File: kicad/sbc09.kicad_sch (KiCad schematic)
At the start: 77 parts, among them J1 Conn_01x03_Male, J2 Conn_01x06_Male, J3 Conn_01x06_Male, J4 Conn_01x06_Male, J5 Conn_02x05_Odd_Even, J6 Conn_02x25_Odd_Even, Q1 2N7000, SW1 SW_Push, U1 74LS245, U10 74LS670, U11 74LS670, U12 AS6C4008-55PCN, U13 SST39SF040-DIP, U14 SST39SF040-DIP, U15 XR68C681CJ, U16 MAX232, U2 74LS245, U3 74LS245, U4 MC6809E, U5 74HCT125, U6 ATF22V10C, U7 ATF22V10C, U8 74LS670, U9 74LS670, X1 8MHz, X2 3.6864MHz

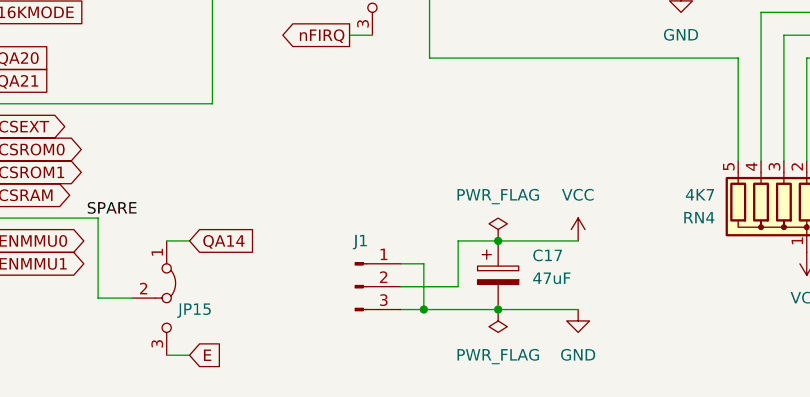
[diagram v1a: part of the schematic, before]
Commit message: Replace J1 (ext power) with Molex KK
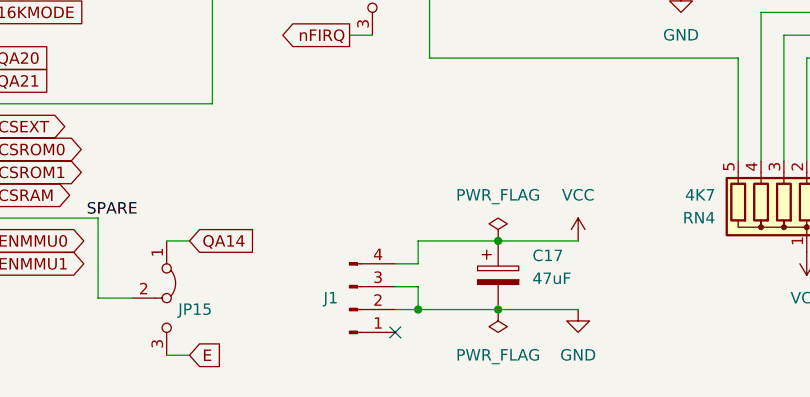
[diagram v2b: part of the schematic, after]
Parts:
- removed J1: Conn_01x03_Male, Connector_PinHeader_2.54mm:PinHeader_1x03_P2.54mm_Vertical, symbol Connector:Conn_01x03_Male
- added J1: (no value), symbol Connector:Conn_01x04_Male
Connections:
- net GND: now also J1.2 (Pin_2), J1.3 (Pin_3)
- net VCC: now also J1.4 (Pin_4)
- no-connect marks 15 -> 16
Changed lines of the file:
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@@
   (junction (at 35.56 34.29) (diameter 0) (color 0 0 0 0)
   )
+  (junction (at 125.73 276.86) (diameter 0) (color 0 0 0 0)
+  )
   (junction (at 156.21 19.05) (diameter 0) (color 0 0 0 0)
   )
@@
   (junction (at 26.67 40.64) (diameter 0) (color 0 0 0 0)
   )
-  (junction (at 126.365 276.86) (diameter 0) (color 0 0 0 0)
-  )
   (junction (at 33.02 166.37) (diameter 0) (color 0 0 0 0)
   )
@@
   (junction (at 246.38 248.92) (diameter 0) (color 0 0 0 0)
   )
+  (no_connect (at 123.19 279.4))
   (no_connect (at 377.19 219.71))
   (no_connect (at 129.54 231.14))
@@
     (stroke (width 0) (type default) (color 0 0 0 0))
   )
-  (wire (pts (xy 227.33 256.54) (xy 240.03 256.54))
+  (wire (pts (xy 125.73 269.24) (xy 134.62 269.24))
     (stroke (width 0) (type default) (color 0 0 0 0))
   )
-  (wire (pts (xy 130.175 269.24) (xy 134.62 269.24))
+  (wire (pts (xy 227.33 256.54) (xy 240.03 256.54))
     (stroke (width 0) (type default) (color 0 0 0 0))
   )
@@
     (stroke (width 0) (type default) (color 0 0 0 0))
   )
+  (wire (pts (xy 125.73 271.78) (xy 125.73 269.24))
+    (stroke (width 0) (type default) (color 0 0 0 0))
+  )
   (wire (pts (xy 195.58 218.44) (xy 217.17 218.44))
     (stroke (width 0) (type default) (color 0 0 0 0))
@@
     (stroke (width 0) (type default) (color 0 0 0 0))
   )
-  (wire (pts (xy 123.825 276.86) (xy 126.365 276.86))
-    (stroke (width 0) (type default) (color 0 0 0 0))
-  )
   (wire (pts (xy 389.89 219.71) (xy 400.05 219.71))
     (stroke (width 0) (type default) (color 0 0 0 0))
@@
     (stroke (width 0) (type default) (color 0 0 0 0))
   )
-  (wire (pts (xy 130.175 274.32) (xy 123.825 274.32))
-    (stroke (width 0) (type default) (color 0 0 0 0))
-  )
   (wire (pts (xy 302.26 180.34) (xy 302.26 181.61))
     (stroke (width 0) (type default) (color 0 0 0 0))
@@
     (stroke (width 0) (type default) (color 0 0 0 0))
   )
-  (wire (pts (xy 126.365 276.86) (xy 134.62 276.86))
-    (stroke (width 0) (type default) (color 0 0 0 0))
-  )
   (wire (pts (xy 295.91 73.66) (xy 312.42 73.66))
     (stroke (width 0) (type default) (color 0 0 0 0))
@@
     (stroke (width 0) (type default) (color 0 0 0 0))
   )
+  (wire (pts (xy 123.19 274.32) (xy 125.73 274.32))
+    (stroke (width 0) (type default) (color 0 0 0 0))
+  )
   (wire (pts (xy 52.07 78.74) (xy 48.26 78.74))
     (stroke (width 0) (type default) (color 0 0 0 0))
@@
     (stroke (width 0) (type default) (color 0 0 0 0))
   )
+  (wire (pts (xy 123.19 271.78) (xy 125.73 271.78))
+    (stroke (width 0) (type default) (color 0 0 0 0))
+  )
   (wire (pts (xy 337.82 53.34) (xy 342.9 53.34))
     (stroke (width 0) (type default) (color 0 0 0 0))
@@
     (stroke (width 0) (type default) (color 0 0 0 0))
   )
+  (wire (pts (xy 125.73 276.86) (xy 134.62 276.86))
+    (stroke (width 0) (type default) (color 0 0 0 0))
+  )
   (wire (pts (xy 100.33 269.24) (xy 97.79 269.24))
     (stroke (width 0) (type default) (color 0 0 0 0))
@@
     (stroke (width 0) (type default) (color 0 0 0 0))
   )
+  (wire (pts (xy 125.73 274.32) (xy 125.73 276.86))
+    (stroke (width 0) (type default) (color 0 0 0 0))
+  )
   (wire (pts (xy 340.36 71.12) (xy 337.82 71.12))
     (stroke (width 0) (type default) (color 0 0 0 0))
@@
     (stroke (width 0) (type default) (color 0 0 0 0))
   )
-  (wire (pts (xy 123.825 271.78) (xy 126.365 271.78))
-    (stroke (width 0) (type default) (color 0 0 0 0))
-  )
   (wire (pts (xy 26.67 40.64) (xy 17.78 40.64))
     (stroke (width 0) (type default) (color 0 0 0 0))
@@
     (stroke (width 0) (type default) (color 0 0 0 0))
   )
+  (wire (pts (xy 123.19 276.86) (xy 125.73 276.86))
+    (stroke (width 0) (type default) (color 0 0 0 0))
+  )
   (bus (pts (xy 369.57 176.53) (xy 369.57 179.07))
     (stroke (width 0) (type default) (color 0 0 0 0))
@@
     (stroke (width 0) (type default) (color 0 0 0 0))
   )
-  (wire (pts (xy 126.365 271.78) (xy 126.365 276.86))
-    (stroke (width 0) (type default) (color 0 0 0 0))
-  )
   (wire (pts (xy 396.24 50.8) (xy 401.32 50.8))
     (stroke (width 0) (type default) (color 0 0 0 0))
@@
     (stroke (width 0) (type default) (color 0 0 0 0))
   )
-  (wire (pts (xy 130.175 274.32) (xy 130.175 269.24))
-    (stroke (width 0) (type default) (color 0 0 0 0))
-  )
   (bus (pts (xy 208.28 38.1) (xy 208.28 40.64))
     (stroke (width 0) (type default) (color 0 0 0 0))
@@
     (pin "1")
   )
-  (symbol (lib_id "Connector:Conn_01x03_Male") (at 118.745 274.32 0) (unit 1)
-    (in_bom yes) (on_board yes) (fields_autoplaced)
-    (property "Reference" "J1" (id 0) (at 119.38 269.24 0))
-    (property "Value" "Conn_01x03_Male" (id 1) (at 119.38 269.24 0)
-      (effects (font (size 1.27 1.27)) hide)
-    )
-    (property "Footprint" "Connector_PinHeader_2.54mm:PinHeader_1x03_P2.54mm_Vertical" (id 2) (at 118.745 274.32 0)
-      (effects (font (size 1.27 1.27)) hide)
-    )
-    (property "Datasheet" "~" (id 3) (at 118.745 274.32 0)
-      (effects (font (size 1.27 1.27)) hide)
-    )
-    (pin "1")
-    (pin "2")
-    (pin "3")
-  )
   (symbol (lib_id "power:GND") (at 185.42 269.24 0) (unit 1)
     (in_bom yes) (on_board yes) (fields_autoplaced)
@@
     (pin "3")
   )
+  (symbol (lib_id "Connector:Conn_01x04_Male") (at 118.11 276.86 0) (mirror x) (unit 1)
+    (in_bom yes) (on_board yes) (fields_autoplaced)
+    (property "Reference" "J1" (id 0) (at 116.84 275.5899 0)
+      (effects (font (size 1.27 1.27)) (justify right))
+    )
+    (property "Value" "" (id 1) (at 118.745 281.94 0)
+      (effects (font (size 1.27 1.27)) hide)
+    )
+    (property "Footprint" "" (id 2) (at 118.11 276.86 0)
+      (effects (font (size 1.27 1.27)) hide)
+    )
+    (property "Datasheet" "~" (id 3) (at 118.11 276.86 0)
+      (effects (font (size 1.27 1.27)) hide)
+    )
+    (pin "1")
+    (pin "2")
+    (pin "3")
+    (pin "4")
+  )
   (symbol (lib_id "Device:R_Network08") (at 25.4 105.41 90) (mirror x) (unit 1)
     (in_bom yes) (on_board yes)
@@
       (reference "H4") (unit 1) (value "2.7mm") (footprint "MountingHole:MountingHole_2.7mm")
     )
-    (path "/2d3bef94-9857-4263-bb09-146a0d34f7ef"
-      (reference "J1") (unit 1) (value "Conn_01x03_Male") (footprint "Connector_PinHeader_2.54mm:PinHeader_1x03_P2.54mm_Vertical")
+    (path "/d7ab0ff9-7261-48ad-92eb-b63b9921aed9"
+      (reference "J1") (unit 1) (value "Conn_01x04_Male") (footprint "Connector_Molex:Molex_KK-254_AE-6410-04A_1x04_P2.54mm_Vertical")
     )
     (path "/c8679364-5ecf-4ff5-92b0-70a3c93f3773"

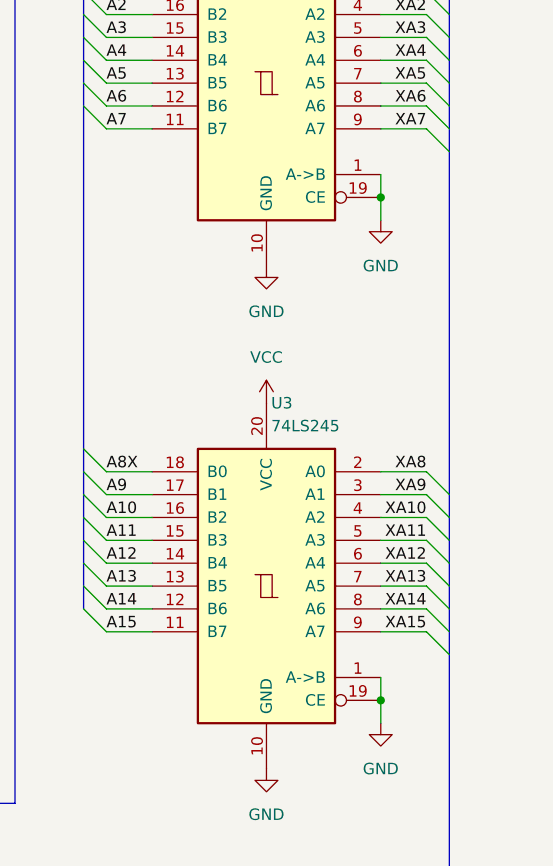
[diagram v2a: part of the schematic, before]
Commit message: Control direction of Addr buffers from BA
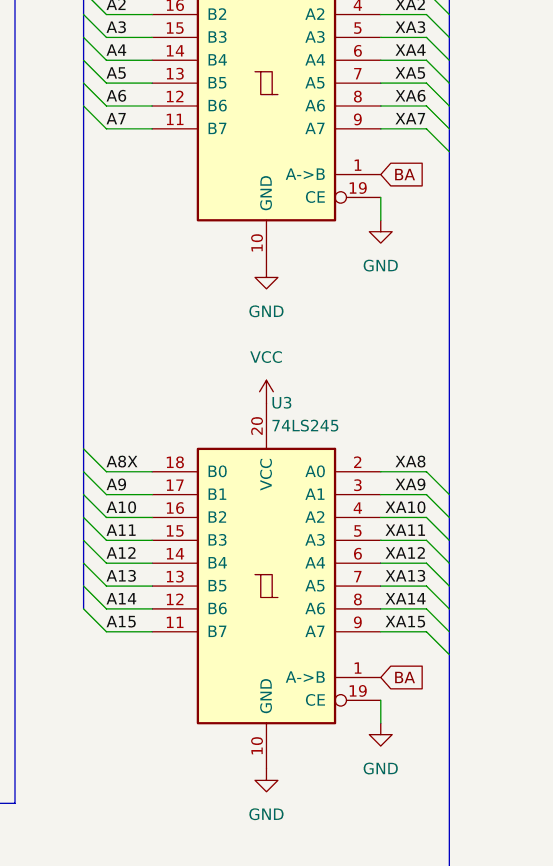
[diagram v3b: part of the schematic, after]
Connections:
- net BA: now also U2.1 (A->B), U3.1 (A->B)
- net GND: no longer U2.1 (A->B), U3.1 (A->B)
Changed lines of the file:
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@@
   (junction (at 246.38 256.54) (diameter 0) (color 0 0 0 0)
   )
-  (junction (at 396.24 60.96) (diameter 0) (color 0 0 0 0)
-  )
   (junction (at 264.16 154.305) (diameter 0) (color 0 0 0 0)
   )
@@
   (junction (at 74.93 153.67) (diameter 0) (color 0 0 0 0)
   )
-  (junction (at 396.24 116.84) (diameter 0) (color 0 0 0 0)
-  )
   (junction (at 240.03 270.51) (diameter 0) (color 0 0 0 0)
   )
@@
     (stroke (width 0) (type default) (color 0 0 0 0))
   )
-  (wire (pts (xy 396.24 114.3) (xy 396.24 116.84))
-    (stroke (width 0) (type default) (color 0 0 0 0))
-  )
   (bus (pts (xy 256.54 40.64) (xy 256.54 43.18))
     (stroke (width 0) (type default) (color 0 0 0 0))
@@
     (stroke (width 0) (type default) (color 0 0 0 0))
   )
-  (wire (pts (xy 396.24 58.42) (xy 396.24 60.96))
-    (stroke (width 0) (type default) (color 0 0 0 0))
-  )
   (wire (pts (xy 49.53 96.52) (xy 52.07 96.52))
     (stroke (width 0) (type default) (color 0 0 0 0))
@@
     )
   )
+  (global_label "BA" (shape input) (at 396.24 58.42 0) (fields_autoplaced)
+    (effects (font (size 1.27 1.27)) (justify left))
+    (property "Intersheet References" "${INTERSHEET_REFS}" (id 0) (at 401.0117 58.3406 0)
+      (effects (font (size 1.27 1.27)) (justify left) hide)
+    )
+  )
   (global_label "Q" (shape input) (at 49.53 99.06 180) (fields_autoplaced)
     (effects (font (size 1.27 1.27)) (justify right))
@@
       (effects (font (size 1.27 1.27)) (justify left) hide)
     )
+  )
+  (global_label "BA" (shape input) (at 396.24 114.3 0) (fields_autoplaced)
+    (effects (font (size 1.27 1.27)) (justify left))
+    (property "Intersheet References" "${INTERSHEET_REFS}" (id 0) (at 401.0117 114.2206 0)
+      (effects (font (size 1.27 1.27)) (justify left) hide)
+    )

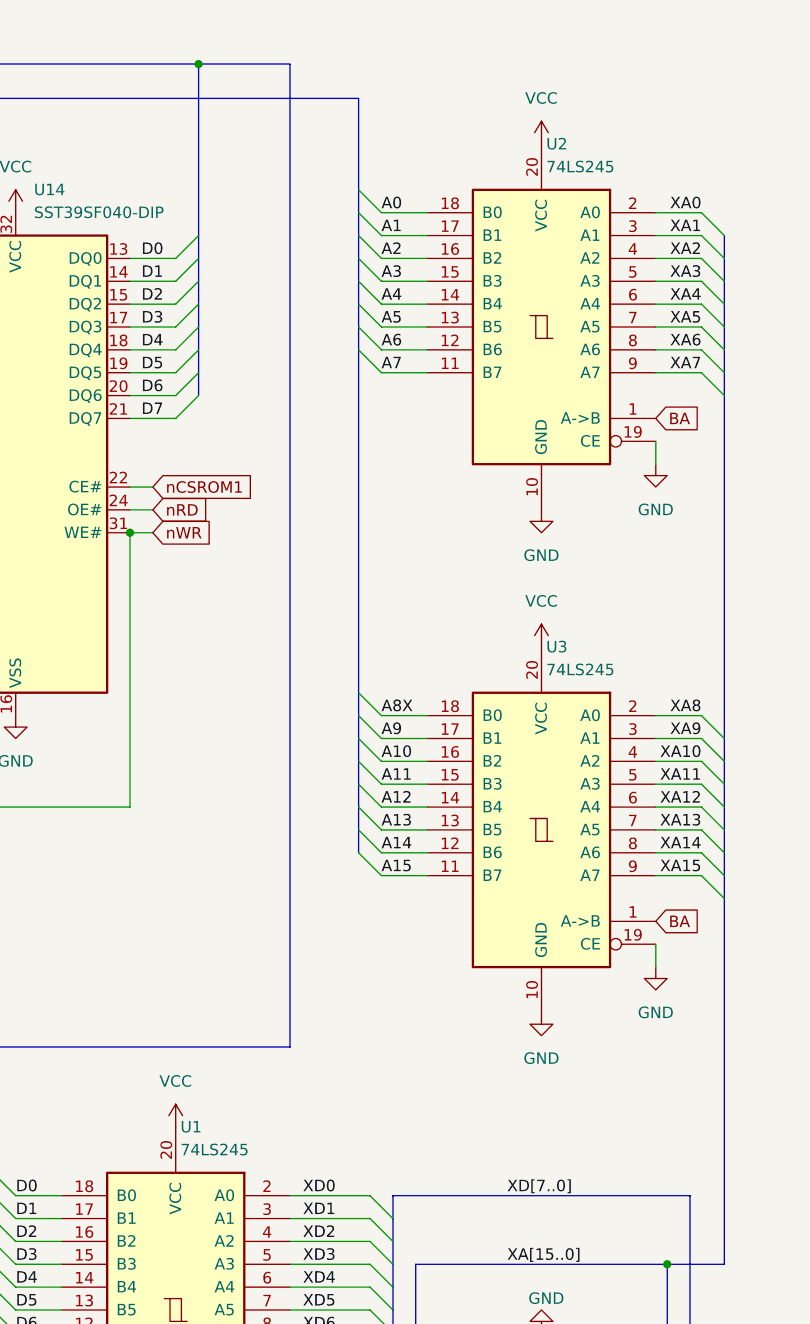
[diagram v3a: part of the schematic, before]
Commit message: Change value of U1/2/3 to 74HCT245
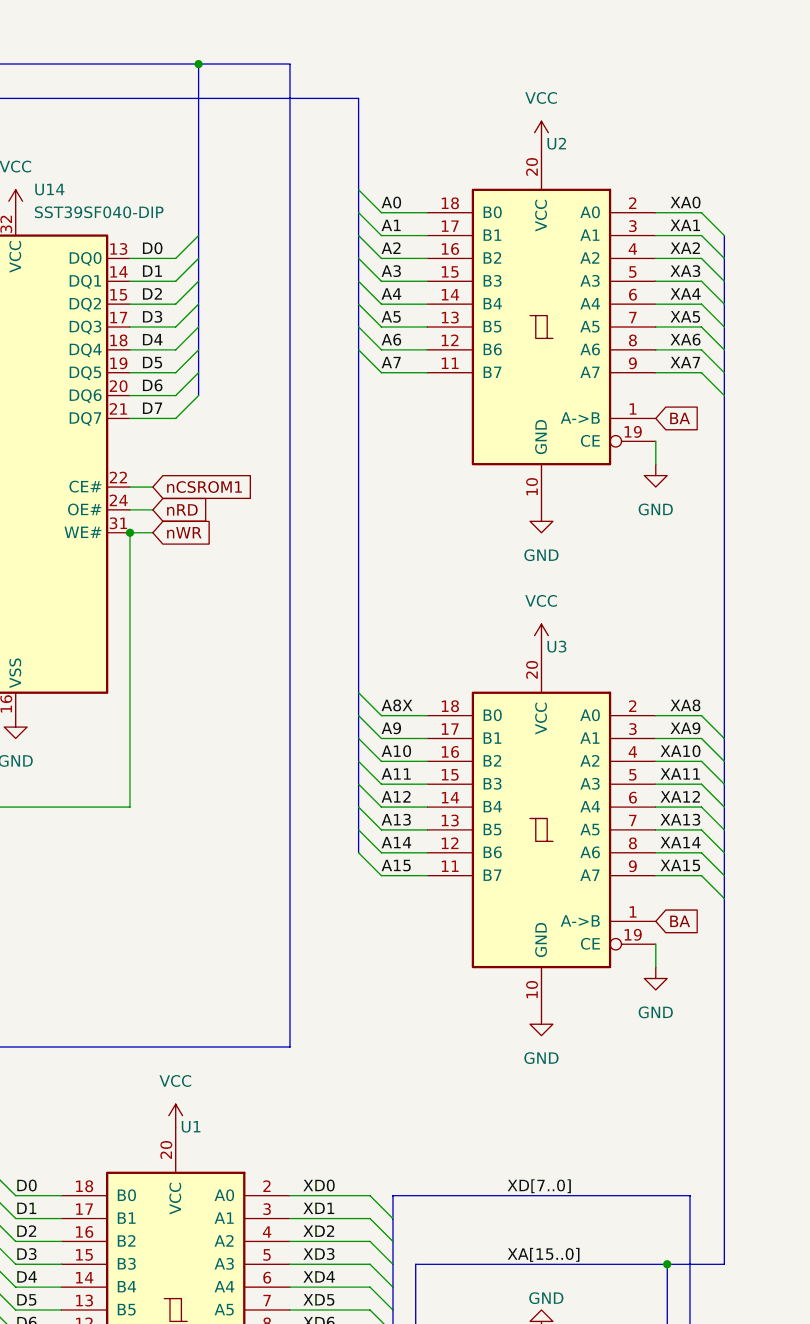
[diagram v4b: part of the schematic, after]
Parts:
- U1, U2, U3: value 74LS245 -> (none)
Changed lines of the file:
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@@
       (effects (font (size 1.27 1.27)) (justify right))
     )
-    (property "Value" "74LS245" (id 1) (at 384.0606 86.36 0)
+    (property "Value" "" (id 1) (at 384.0606 86.36 0)
       (effects (font (size 1.27 1.27)) (justify right))
     )
@@
       (effects (font (size 1.27 1.27)) (justify right))
     )
-    (property "Value" "74LS245" (id 1) (at 384.0606 30.48 0)
+    (property "Value" "" (id 1) (at 384.0606 30.48 0)
       (effects (font (size 1.27 1.27)) (justify right))
     )
@@
       (effects (font (size 1.27 1.27)) (justify right))
     )
-    (property "Value" "74LS245" (id 1) (at 343.4206 139.7 0)
+    (property "Value" "" (id 1) (at 343.4206 139.7 0)
       (effects (font (size 1.27 1.27)) (justify right))
     )
@@
     )
     (path "/b94ab99f-52e3-4ccf-b6fb-e7021a9f054f"
-      (reference "U1") (unit 1) (value "74LS245") (footprint "Package_DIP:DIP-20_W7.62mm_Socket")
+      (reference "U1") (unit 1) (value "74HCT245") (footprint "Package_DIP:DIP-20_W7.62mm_Socket")
     )
     (path "/ac5972a1-fe98-469b-83c0-ddd983b35429"
-      (reference "U2") (unit 1) (value "74LS245") (footprint "Package_DIP:DIP-20_W7.62mm_Socket")
+      (reference "U2") (unit 1) (value "74HCT245") (footprint "Package_DIP:DIP-20_W7.62mm_Socket")
     )
     (path "/8faef091-bd23-44f5-86d7-3dbb33eb4c2b"
-      (reference "U3") (unit 1) (value "74LS245") (footprint "Package_DIP:DIP-20_W7.62mm_Socket")
+      (reference "U3") (unit 1) (value "74HCT245") (footprint "Package_DIP:DIP-20_W7.62mm_Socket")
     )
     (path "/625a12c3-d955-4962-8e19-1bdba92d86fb"

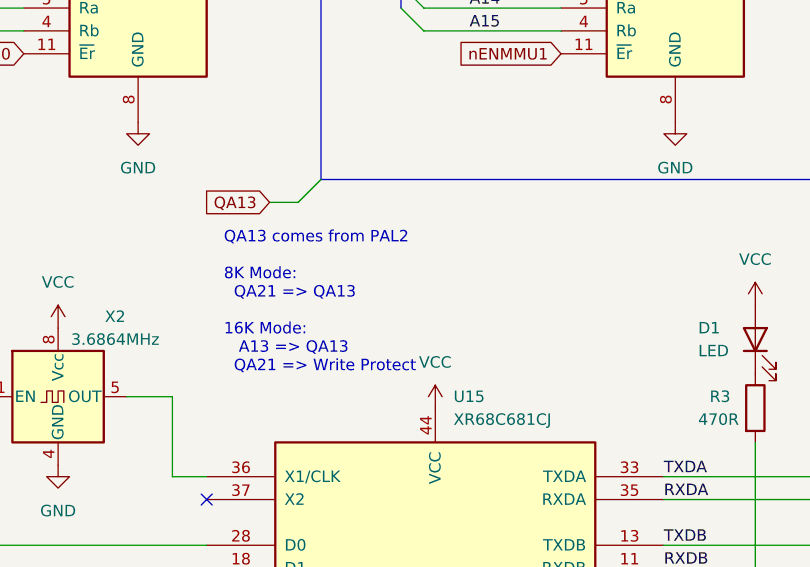
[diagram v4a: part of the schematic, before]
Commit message: Correct comment on schematic
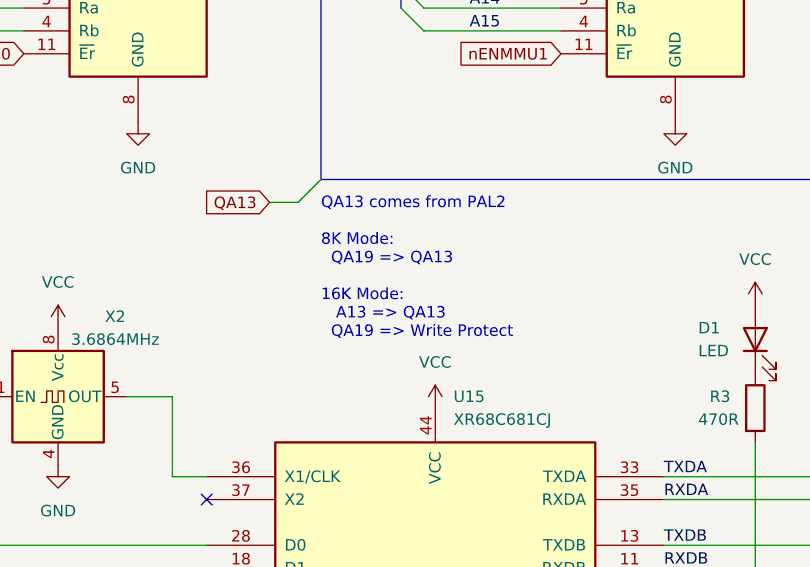
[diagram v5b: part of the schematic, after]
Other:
- note added: "QA13 comes from PAL2 8K Mode: QA19 => QA13 16K Mode: A13 => QA13 QA19 => Write Protect"
- note removed: "QA13 comes from PAL2 8K Mode: QA21 => QA13 16K Mode: A13 => QA13 QA21 => Write Protect"
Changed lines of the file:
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@@
     (effects (font (size 1.27 1.27)) (justify left bottom))
   )
-  (text "QA13 comes from PAL2\n\n8K Mode:\n  QA21 => QA13\n\n16K Mode:\n   A13 => QA13\n  QA21 => Write Protect\n"
-    (at 131.445 163.83 0)
+  (text "QA13 comes from PAL2\n\n8K Mode:\n  QA19 => QA13\n\n16K Mode:\n   A13 => QA13\n  QA19 => Write Protect\n"
+    (at 142.24 160.02 0)
     (effects (font (size 1.27 1.27)) (justify left bottom))
   )

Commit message: KiCAD: Added PAL3 and updated layout
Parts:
- added U17: GAL16V8, Package_DIP:DIP-20_W7.62mm_Socket, symbol Logic_Programmable:GAL16V8
- J1: value (none) -> Conn_01x04_Male; footprint (none) -> Connector_Molex:Molex_KK-254_AE-6410-04A_1x04_P2.54mm_Vertical
- U1, U2, U3: value (none) -> 74HCT245
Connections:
- net 16KMODE: now also U7.2 (I0); no longer U7.13 (CLK/OD)
- net A10: now also U17.5 (I5); no longer U7.6 (I4)
- net A11: now also U17.6 (I6); no longer U7.7 (I5)
- net A12: now also U17.7 (I7); no longer U7.8 (I6)
- net A13: now also U17.8 (I8); no longer U6.9 (I7)
- net A14: now also U17.9 (I9)
- net A15: now also U17.11 (I10/~{OE})
- net A6: now also U17.1 (I1/CLK); no longer U7.2 (I0)
- net A7: now also U17.2 (I2); no longer U7.3 (I1)
- net A8: now also U17.3 (I3); no longer U7.4 (I2)
- net A9: now also U17.4 (I4); no longer U7.5 (I3)
- net GND: now also U17.10 (GND)
- net QA13: now also U7.23 (O0/LR); no longer U6.14 (LR/O4)
- net QA14: now also U7.22 (O1/A0); no longer JP15.1 (A)
- net QA19: now also U7.3 (I1)
- net QA20: now also U7.4 (I2); no longer U7.23 (O0/LR)
- net QA21: now also U7.5 (I3); no longer U7.22 (O1/A0)
- net VCC: now also U17.20 (VCC)
- net nCSIOINT: now also U7.7 (I5), U17.18 (IO2); no longer U7.21 (O2/A1)
- new net nCSIO: U17.19 (IO1), U7.6 (I4)
- new net nCSIOEXT: U17.17 (I03)
- no-connect marks 16 -> 27
